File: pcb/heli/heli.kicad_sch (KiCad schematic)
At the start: 32 parts, among them J1 Batterie, J2 Debug, J4 Servo, J5 Servo, Q1 IRLZ44N, SW1 SW_MEC_5E, U1 AZ1117-3.3, U2 MPU-6050, U3 STM32F103CBTx, Y1 8MHz

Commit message: 
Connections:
- net GPS_CSN: now also U3.22 (PB11); no longer U3.40 (PB4)
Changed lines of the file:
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@@
     )
   )
-  (global_label "GPS_CSN" (shape output) (at 136.525 77.47 180) (fields_autoplaced)
+  (global_label "GPS_CSN" (shape output) (at 136.525 95.25 180) (fields_autoplaced)
     (effects (font (size 1.27 1.27)) (justify right))
-    (property "Intersheet References" "${INTERSHEET_REFS}" (id 0) (at 125.5848 77.3906 0)
+    (property "Intersheet References" "${INTERSHEET_REFS}" (id 0) (at 125.5848 95.1706 0)
       (effects (font (size 1.27 1.27)) (justify right) hide)
     )

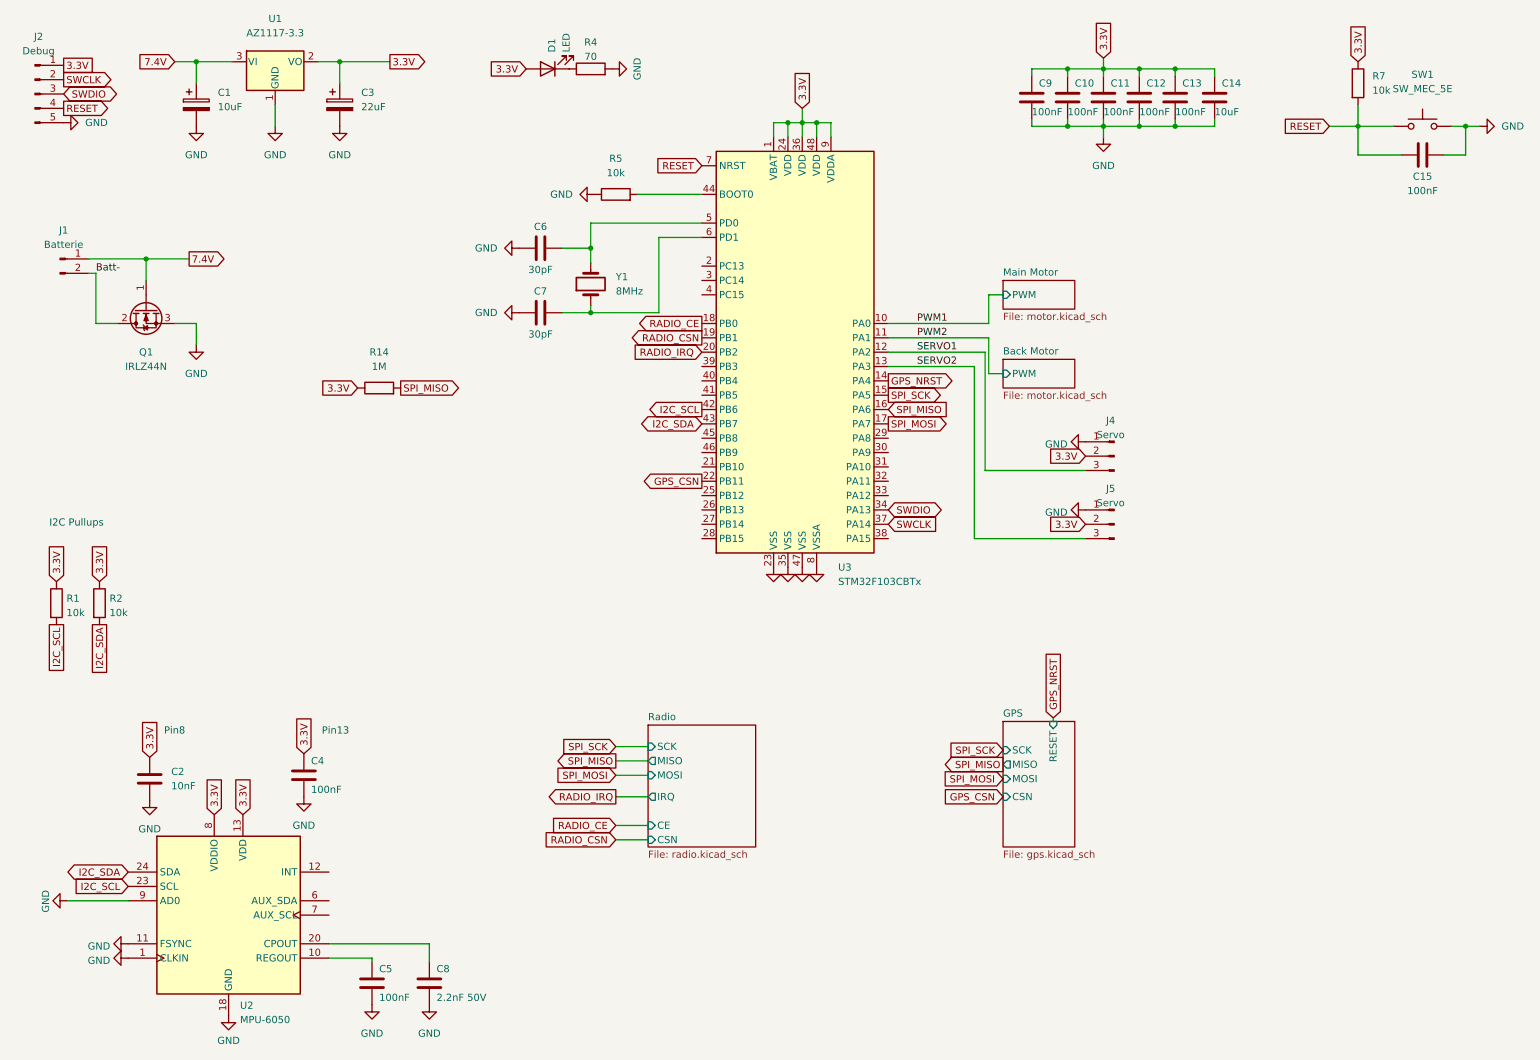
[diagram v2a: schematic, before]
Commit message: Added BMI270 to schematic and SPI2 to the code
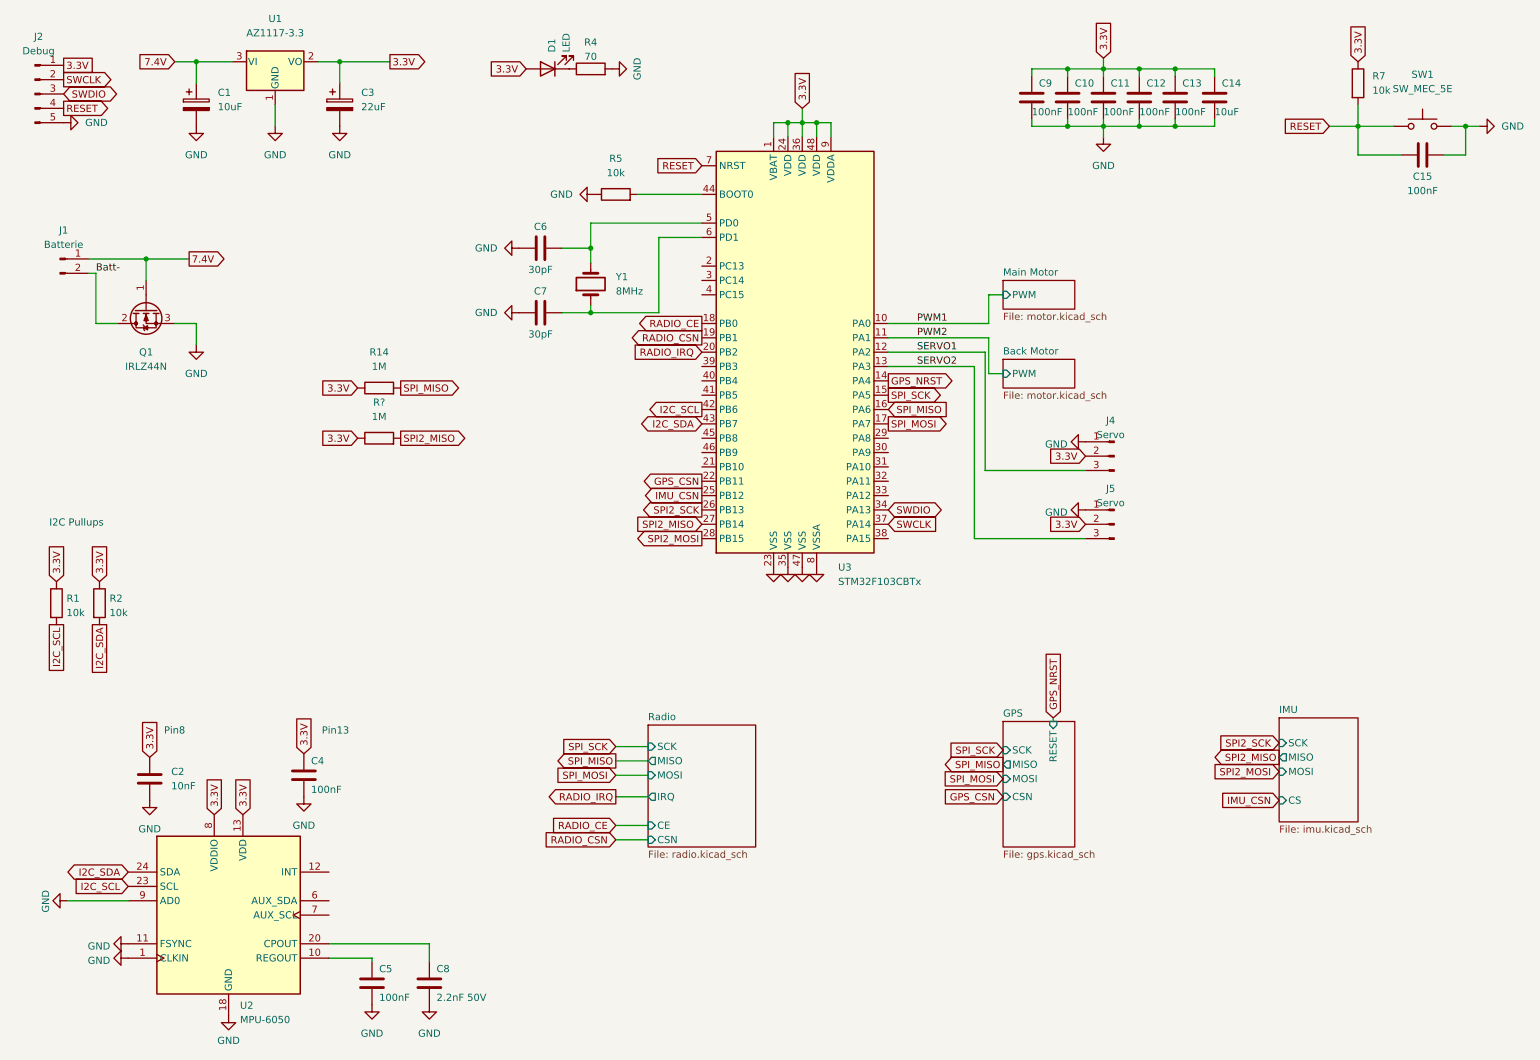
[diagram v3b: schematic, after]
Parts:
- added R?: 1M, Resistor_SMD:R_0603_1608Metric, symbol Device:R
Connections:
- net 3.3V: now also R?.1
- net IMU_CSN: now reaches U3.25 (PB12)
- net SPI2_SCK: now reaches U3.26 (PB13)
- net SPI2_MISO: now reaches U3.27 (PB14)
- net SPI2_MISO: now also R?.2
- net SPI2_MOSI: now reaches U3.28 (PB15)
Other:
- added sheet IMU (imu.kicad_sch)
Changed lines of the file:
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@@
     (effects (font (size 1.27 1.27)) (justify left bottom))
   )
+  (global_label "SPI2_SCK" (shape input) (at 238.76 141.605 180) (fields_autoplaced)
+    (effects (font (size 1.27 1.27)) (justify right))
+    (property "Intersheet References" "${INTERSHEET_REFS}" (id 0) (at 227.3359 141.5256 0)
+      (effects (font (size 1.27 1.27)) (justify right) hide)
+    )
+  )
   (global_label "GPS_CSN" (shape input) (at 189.865 151.13 180) (fields_autoplaced)
     (effects (font (size 1.27 1.27)) (justify right))
@@
     )
   )
+  (global_label "SPI2_SCK" (shape output) (at 136.525 100.33 180) (fields_autoplaced)
+    (effects (font (size 1.27 1.27)) (justify right))
+    (property "Intersheet References" "${INTERSHEET_REFS}" (id 0) (at 125.1009 100.2506 0)
+      (effects (font (size 1.27 1.27)) (justify right) hide)
+    )
+  )
   (global_label "RESET" (shape input) (at 136.525 39.37 180) (fields_autoplaced)
     (effects (font (size 1.27 1.27)) (justify right))
@@
     )
   )
+  (global_label "IMU_CSN" (shape input) (at 238.76 151.765 180) (fields_autoplaced)
+    (effects (font (size 1.27 1.27)) (justify right))
+    (property "Intersheet References" "${INTERSHEET_REFS}" (id 0) (at 228.1826 151.6856 0)
+      (effects (font (size 1.27 1.27)) (justify right) hide)
+    )
+  )
   (global_label "I2C_SCL" (shape output) (at 136.525 82.55 180) (fields_autoplaced)
     (effects (font (size 1.27 1.27)) (justify right))
@@
     )
   )
+  (global_label "SPI2_MISO" (shape output) (at 238.76 144.145 180) (fields_autoplaced)
+    (effects (font (size 1.27 1.27)) (justify right))
+    (property "Intersheet References" "${INTERSHEET_REFS}" (id 0) (at 226.4893 144.0656 0)
+      (effects (font (size 1.27 1.27)) (justify right) hide)
+    )
+  )
   (global_label "3.3V" (shape input) (at 22.225 113.03 90) (fields_autoplaced)
     (effects (font (size 1.27 1.27)) (justify left))
@@
     )
   )
+  (global_label "3.3V" (shape input) (at 75.565 87.63 180) (fields_autoplaced)
+    (effects (font (size 1.27 1.27)) (justify right))
+    (property "Intersheet References" "${INTERSHEET_REFS}" (id 0) (at 69.0395 87.7094 0)
+      (effects (font (size 1.27 1.27)) (justify right) hide)
+    )
+  )
   (global_label "GPS_CSN" (shape output) (at 136.525 95.25 180) (fields_autoplaced)
     (effects (font (size 1.27 1.27)) (justify right))
@@
     )
   )
+  (global_label "SPI2_MOSI" (shape output) (at 136.525 105.41 180) (fields_autoplaced)
+    (effects (font (size 1.27 1.27)) (justify right))
+    (property "Intersheet References" "${INTERSHEET_REFS}" (id 0) (at 124.2543 105.3306 0)
+      (effects (font (size 1.27 1.27)) (justify right) hide)
+    )
+  )
   (global_label "3.3V" (shape input) (at 105.41 22.225 180) (fields_autoplaced)
     (effects (font (size 1.27 1.27)) (justify right))
@@
     )
   )
+  (global_label "IMU_CSN" (shape output) (at 136.525 97.79 180) (fields_autoplaced)
+    (effects (font (size 1.27 1.27)) (justify right))
+    (property "Intersheet References" "${INTERSHEET_REFS}" (id 0) (at 125.9476 97.7106 0)
+      (effects (font (size 1.27 1.27)) (justify right) hide)
+    )
+  )
   (global_label "3.3V" (shape input) (at 154.305 29.21 90) (fields_autoplaced)
     (effects (font (size 1.27 1.27)) (justify left))
@@
     )
   )
+  (global_label "SPI2_MOSI" (shape input) (at 238.76 146.685 180) (fields_autoplaced)
+    (effects (font (size 1.27 1.27)) (justify right))
+    (property "Intersheet References" "${INTERSHEET_REFS}" (id 0) (at 226.4893 146.6056 0)
+      (effects (font (size 1.27 1.27)) (justify right) hide)
+    )
+  )
   (global_label "SPI_SCK" (shape input) (at 189.865 142.875 180) (fields_autoplaced)
     (effects (font (size 1.27 1.27)) (justify right))
@@
     )
   )
+  (global_label "SPI2_MISO" (shape output) (at 83.185 87.63 0) (fields_autoplaced)
+    (effects (font (size 1.27 1.27)) (justify left))
+    (property "Intersheet References" "${INTERSHEET_REFS}" (id 0) (at 95.4557 87.5506 0)
+      (effects (font (size 1.27 1.27)) (justify left) hide)
+    )
+  )
   (global_label "GPS_NRST" (shape output) (at 169.545 77.47 0) (fields_autoplaced)
     (effects (font (size 1.27 1.27)) (justify left))
@@
     (property "Intersheet References" "${INTERSHEET_REFS}" (id 0) (at 55.1656 147.7795 90)
       (effects (font (size 1.27 1.27)) (justify left) hide)
+    )
+  )
+  (global_label "SPI2_MISO" (shape input) (at 136.525 102.87 180) (fields_autoplaced)
+    (effects (font (size 1.27 1.27)) (justify right))
+    (property "Intersheet References" "${INTERSHEET_REFS}" (id 0) (at 124.2543 102.7906 0)
+      (effects (font (size 1.27 1.27)) (justify right) hide)
     )
   )
@@
     (pin "2")
   )
+  (symbol (lib_id "Device:R") (at 79.375 87.63 90) (unit 1)
+    (in_bom yes) (on_board yes) (fields_autoplaced)
+    (property "Reference" "R?" (id 0) (at 79.375 81.28 90))
+    (property "Value" "1M" (id 1) (at 79.375 83.82 90))
+    (property "Footprint" "Resistor_SMD:R_0603_1608Metric" (id 2) (at 79.375 89.408 90)
+      (effects (font (size 1.27 1.27)) hide)
+    )
+    (property "Datasheet" "~" (id 3) (at 79.375 87.63 0)
+      (effects (font (size 1.27 1.27)) hide)
+    )
+    (property "DIGIKEY" "1292-WR06X105JTLCT-ND" (id 4) (at 79.375 87.63 0)
+      (effects (font (size 1.27 1.27)) hide)
+    )
+    (pin "1")
+    (pin "2")
+  )
   (symbol (lib_id "power:GND") (at 38.735 151.765 0) (unit 1)
     (in_bom yes) (on_board yes) (fields_autoplaced)
@@
     (pin "1")
     (pin "2")
+  )
+  (sheet (at 238.76 137.16) (size 13.97 18.415) (fields_autoplaced)
+    (stroke (width 0.1524) (type solid) (color 0 0 0 0))
+    (fill (color 0 0 0 0.0000))
+    (property "Sheet name" "IMU" (id 0) (at 238.76 136.4484 0)
+      (effects (font (size 1.27 1.27)) (justify left bottom))
+    )
+    (property "Sheet file" "imu.kicad_sch" (id 1) (at 238.76 156.1596 0)
+      (effects (font (size 1.27 1.27)) (justify left top))
+    )
+    (pin "MISO" output (at 238.76 144.145 180)
+      (effects (font (size 1.27 1.27)) (justify left))
+    )
+    (pin "CS" input (at 238.76 151.765 180)
+      (effects (font (size 1.27 1.27)) (justify left))
+    )
+    (pin "SCK" input (at 238.76 141.605 180)
+      (effects (font (size 1.27 1.27)) (justify left))
+    )
+    (pin "MOSI" input (at 238.76 146.685 180)
+      (effects (font (size 1.27 1.27)) (justify left))
+    )
   )
   (sheet (at 127 138.43) (size 19.05 21.59) (fields_autoplaced)
@@
     (path "/ff163e09-1c9a-4e9f-9fc2-cd2f8ec1c6f1" (page "4"))
     (path "/8972c389-56a6-466a-9271-66b0ec918c0e" (page "5"))
+    (path "/24a55773-54fb-43ef-b204-3ed855c51278" (page "6"))
   )
   (symbol_instances
@@
       (reference "#PWR0119") (unit 1) (value "GND") (footprint "")
     )
+    (path "/24a55773-54fb-43ef-b204-3ed855c51278/49e4978f-ee8b-41ca-91a8-4e96ec0b2e0c"
+      (reference "#PWR?") (unit 1) (value "GND") (footprint "")
+    )
+    (path "/24a55773-54fb-43ef-b204-3ed855c51278/5ae4136f-cef7-45de-8038-f39d05d8c052"
+      (reference "#PWR?") (unit 1) (value "GND") (footprint "")
+    )
+    (path "/24a55773-54fb-43ef-b204-3ed855c51278/8feffe42-8b3b-4618-9835-c23e56dfb3f3"
+      (reference "#PWR?") (unit 1) (value "GND") (footprint "")
+    )
+    (path "/24a55773-54fb-43ef-b204-3ed855c51278/cf7bef7f-9921-441e-bb38-fe7eb61da6c7"
+      (reference "#PWR?") (unit 1) (value "GND") (footprint "")
+    )
     (path "/8972c389-56a6-466a-9271-66b0ec918c0e/513d8dee-6e00-4610-92f7-bea566c6ff2b"
       (reference "AE1") (unit 1) (value "Antenna_Shield") (footprint "sparkfun:TRACE_ANTENNA_2.4GHZ_15.2MM")
@@
       (reference "C29") (unit 1) (value "100nF") (footprint "Capacitor_SMD:C_0603_1608Metric")
     )
+    (path "/24a55773-54fb-43ef-b204-3ed855c51278/341ffedd-fb7b-4bc2-9e7e-b7dd4aad6c45"
+      (reference "C?") (unit 1) (value "100nF") (footprint "lib:XDCR_BMI270")
+    )
+    (path "/24a55773-54fb-43ef-b204-3ed855c51278/ab8238fb-a93b-4ebf-8cd2-07cefe467591"
+      (reference "C?") (unit 1) (value "100nF") (footprint "lib:XDCR_BMI270")
+    )
     (path "/b28a0e5f-aecf-489c-9fc5-7ef0cd88e703"
       (reference "D1") (unit 1) (value "LED") (footprint "LED_SMD:LED_0603_1608Metric")
@@
       (reference "R15") (unit 1) (value "10k") (footprint "Resistor_SMD:R_0603_1608Metric")
     )
+    (path "/767f0581-e671-4bc2-b748-641d88ebefbc"
+      (reference "R?") (unit 1) (value "1M") (footprint "Resistor_SMD:R_0603_1608Metric")
+    )
     (path "/adfea837-fd00-47ad-b3eb-1946872908eb"
       (reference "SW1") (unit 1) (value "SW_MEC_5E") (footprint "Button_Switch_SMD:SW_SPST_TL3305A")
@@
       (reference "U5") (unit 1) (value "NRF24L01") (footprint "Package_DFN_QFN:QFN-20-1EP_4x4mm_P0.5mm_EP2.5x2.5mm")
     )
+    (path "/24a55773-54fb-43ef-b204-3ed855c51278/c845ce52-0bfa-4dd7-9e98-262c5b4b03a6"
+      (reference "U?") (unit 1) (value "BMI270") (footprint "XDCR_BMI270")
+    )
     (path "/7167ad50-a0fe-4dd3-bd80-1cc072116538"
